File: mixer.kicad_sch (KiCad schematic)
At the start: 34 parts, among them T1 RF_BALUN, T2 RF_BALUN, U4 RFFC5072

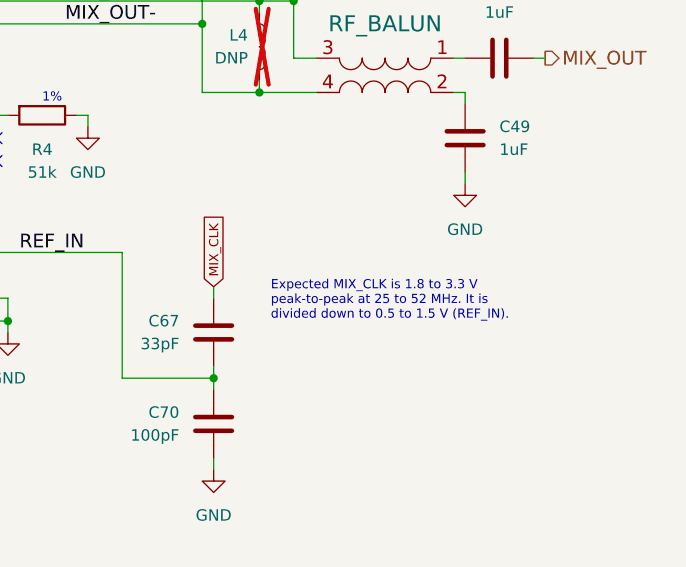
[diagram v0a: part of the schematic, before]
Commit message: Make clock source termination consistent
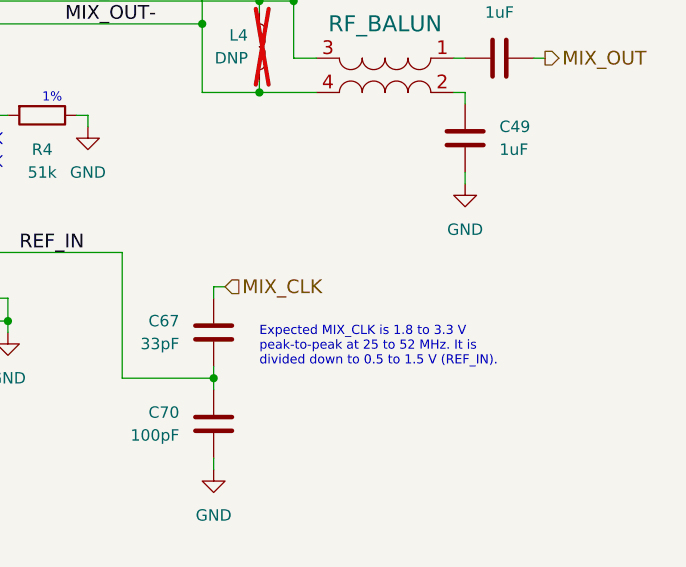
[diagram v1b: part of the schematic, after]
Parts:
- C67: footprint hackrf:GSG-0402 -> Capacitor_SMD:C_0201_0603Metric; Manufacturer Samsung -> Murata; Part Number CL05C330JB5NNNC -> GRM0335C1H330JA01D; Substitution Murata GRM1555C1H330JA01D -> GRM0335C1H330*, GRM0335C1E330*
- C70: footprint hackrf:GSG-0402 -> Capacitor_SMD:C_0201_0603Metric; Manufacturer Samsung -> Murata; Part Number CL05C101JB5NNNC -> GRM0335C1E101JA01D; Substitution Murata GRM1555C1H101JA01D -> GRM0335C1E101JA01*, GRM0335C1H101JA01*
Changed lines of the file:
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@@
 	(wire
 		(pts
+			(xy 151.13 118.11) (xy 152.4 118.11)
+		)
+		(stroke
+			(width 0)
+			(type default)
+		)
+	)
+	(wire
+		(pts
 			(xy 186.69 92.71) (xy 187.96 92.71)
 		)
@@
 	(text "Expected MIX_CLK is 1.8 to 3.3 V\npeak-to-peak at 25 to 52 MHz. It is\ndivided down to 0.5 to 1.5 V (REF_IN)."
 		(exclude_from_sim no)
-		(at 157.48 121.92 0)
+		(at 156.21 127 0)
 		(effects
 			(font
@@
 		)
 	)
-	(global_label "MIX_CLK"
+	(global_label "MIXER_RESETX"
 		(shape input)
-		(at 151.13 118.11 90)
+		(at 49.53 114.3 180)
 		(fields_autoplaced yes)
 		(effects
@@
 				(size 1.016 1.016)
 			)
-			(justify left)
+			(justify right)
 		)
 		(property "Intersheetrefs" "${INTERSHEET_REFS}"
-			(at 151.13 110.0042 90)
+			(at 36.7798 114.3 0)
 			(effects
 				(font
 					(size 1.27 1.27)
 				)
-				(justify left)
+				(justify right)
 				(hide yes)
 			)
 		)
 	)
-	(global_label "MIXER_RESETX"
+	(hierarchical_label "MIX_CLK"
 		(shape input)
-		(at 49.53 114.3 180)
+		(at 152.4 118.11 0)
 		(fields_autoplaced yes)
 		(effects
 			(font
-				(size 1.016 1.016)
-			)
-			(justify right)
-		)
-		(property "Intersheetrefs" "${INTERSHEET_REFS}"
-			(at 36.7798 114.3 0)
-			(effects
-				(font
-					(size 1.27 1.27)
-				)
-				(justify right)
-				(hide yes)
+				(size 1.524 1.524)
 			)
+			(justify left)
 		)
 	)
@@
 			)
 		)
-		(property "Footprint" "hackrf:GSG-0402"
+		(property "Footprint" "Capacitor_SMD:C_0201_0603Metric"
 			(at 151.13 123.19 0)
 			(effects
@@
 			)
 		)
-		(property "Description" "CAP CER 33PF 50V C0G/NP0 0402"
+		(property "Description" "CAP CER 33PF 50V C0G/NP0 0201"
 			(at -137.16 66.04 0)
 			(effects
@@
 			)
 		)
-		(property "Manufacturer" "Samsung"
+		(property "Manufacturer" "Murata"
 			(at -137.16 66.04 0)
 			(effects
@@
 			)
 		)
-		(property "Part Number" "CL05C330JB5NNNC"
+		(property "Part Number" "GRM0335C1H330JA01D"
 			(at -137.16 66.04 0)
 			(effects
@@
 			)
 		)
-		(property "Substitution" "Murata GRM1555C1H330JA01D"
+		(property "Substitution" "GRM0335C1H330*, GRM0335C1E330*"
 			(at 151.13 123.19 0)
 			(effects
@@
 			)
 		)
-		(property "Footprint" "hackrf:GSG-0402"
+		(property "Footprint" "Capacitor_SMD:C_0201_0603Metric"
 			(at 151.13 133.35 0)
 			(effects
@@
 			)
 		)
-		(property "Description" "CAP CER 100PF 50V 5% C0G/NP0 0402"
+		(property "Description" "CAP CER 100PF 25V C0G/NP0 0201"
 			(at 74.93 93.98 0)
 			(effects
@@
 			)
 		)
-		(property "Manufacturer" "Samsung"
+		(property "Manufacturer" "Murata"
 			(at 74.93 93.98 0)
 			(effects
@@
 			)
 		)
-		(property "Part Number" "CL05C101JB5NNNC"
+		(property "Part Number" "GRM0335C1E101JA01D"
 			(at 74.93 93.98 0)
 			(effects
@@
 			)
 		)
-		(property "Substitution" "Murata GRM1555C1H101JA01D"
+		(property "Substitution" "GRM0335C1E101JA01*, GRM0335C1H101JA01*"
 			(at 151.13 133.35 0)
 			(effects

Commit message: Change microcontroller U23 to LPC4330FET180
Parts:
- R5, R6: footprint hackrf:GSG-0402 -> Resistor_SMD:R_0402_1005Metric
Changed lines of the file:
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@@
 			)
 		)
-		(property "Footprint" "hackrf:GSG-0402"
+		(property "Footprint" "Resistor_SMD:R_0402_1005Metric"
 			(at 69.85 109.22 0)
 			(effects
@@
 			)
 		)
-		(property "Footprint" "hackrf:GSG-0402"
+		(property "Footprint" "Resistor_SMD:R_0402_1005Metric"
 			(at 78.74 109.22 0)
 			(effects

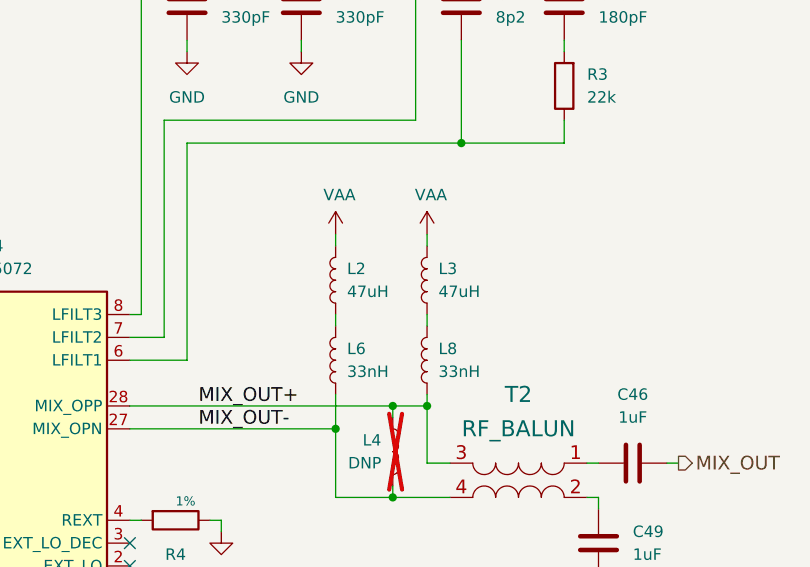
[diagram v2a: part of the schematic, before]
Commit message: Use single 15 uH inductor as RF choke
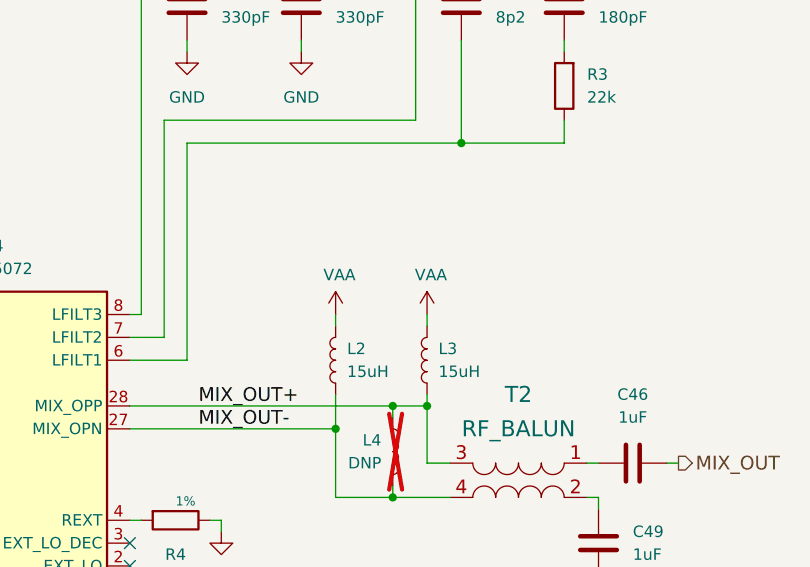
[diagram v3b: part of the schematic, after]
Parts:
- removed L6, L8: 33nH, Inductor_SMD:L_0201_0603Metric, symbol Device:L
- L2, L3: value 47uH -> 15uH; Part Number LSQNB160808T470M -> LSQPB160807T150M; Substitution LSQNB160808T470K -> BRL1608T150M, LLQPB160807T150M
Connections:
- net MIX_OUT+: now also L3.1
- net MIX_OUT-: now also L2.1
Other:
- moved on the sheet: L2, L3

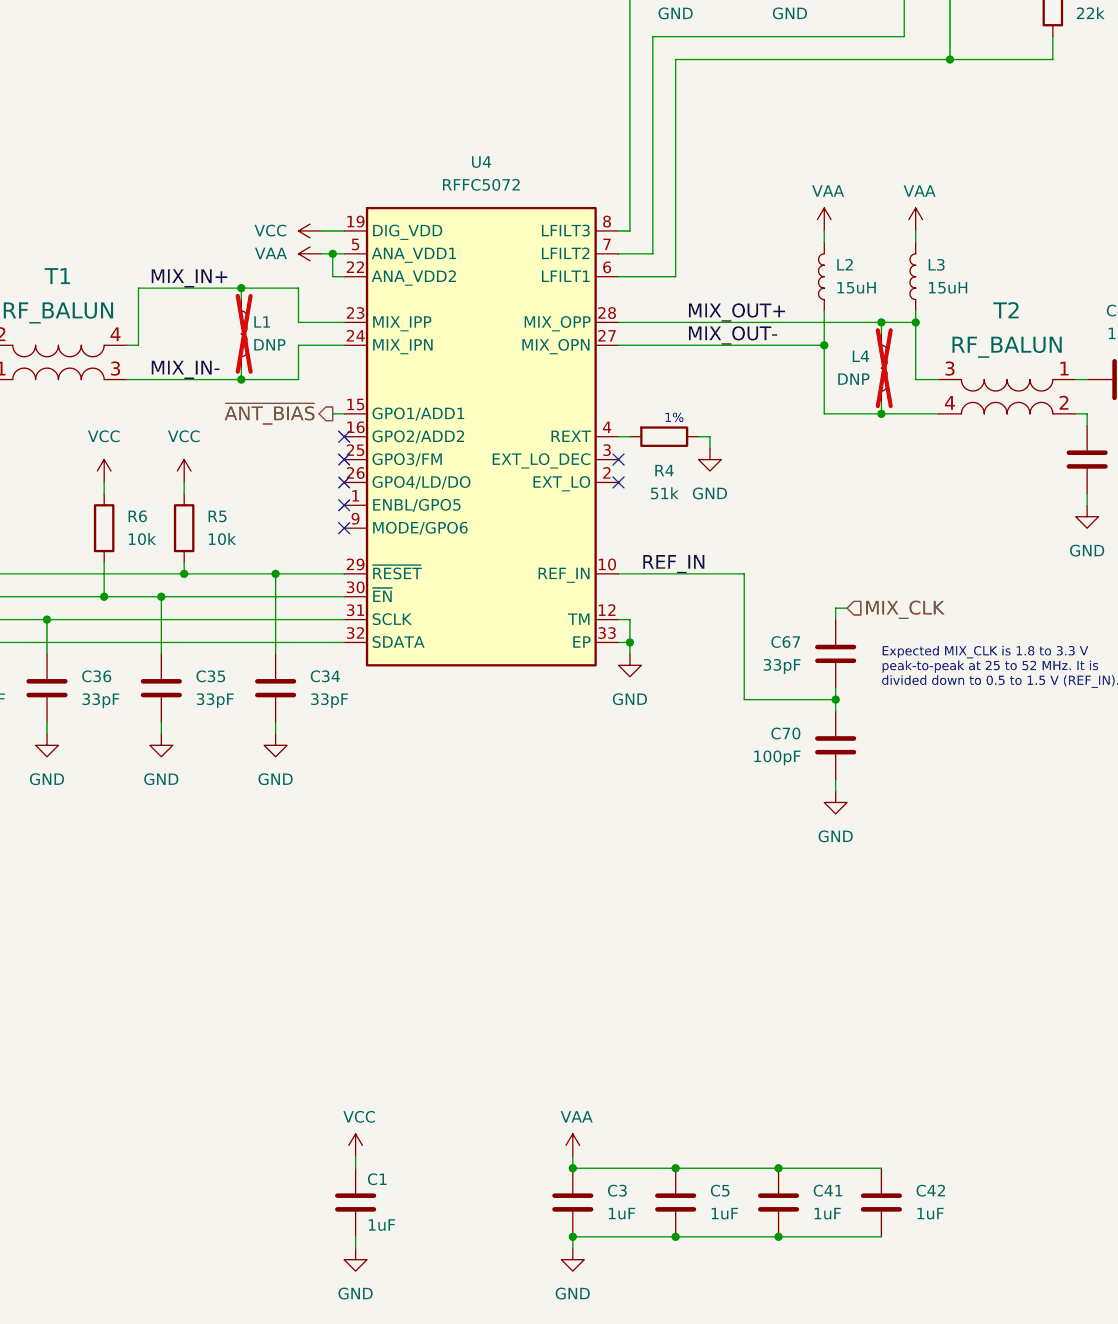
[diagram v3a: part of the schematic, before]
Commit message: Rearrange RF section
- Use DPDT RF switches to reduce long tracks
- Add limiter
- Add switch control logic
- Move ADC/DAC U18 to RF area
- Remove baseband header P9
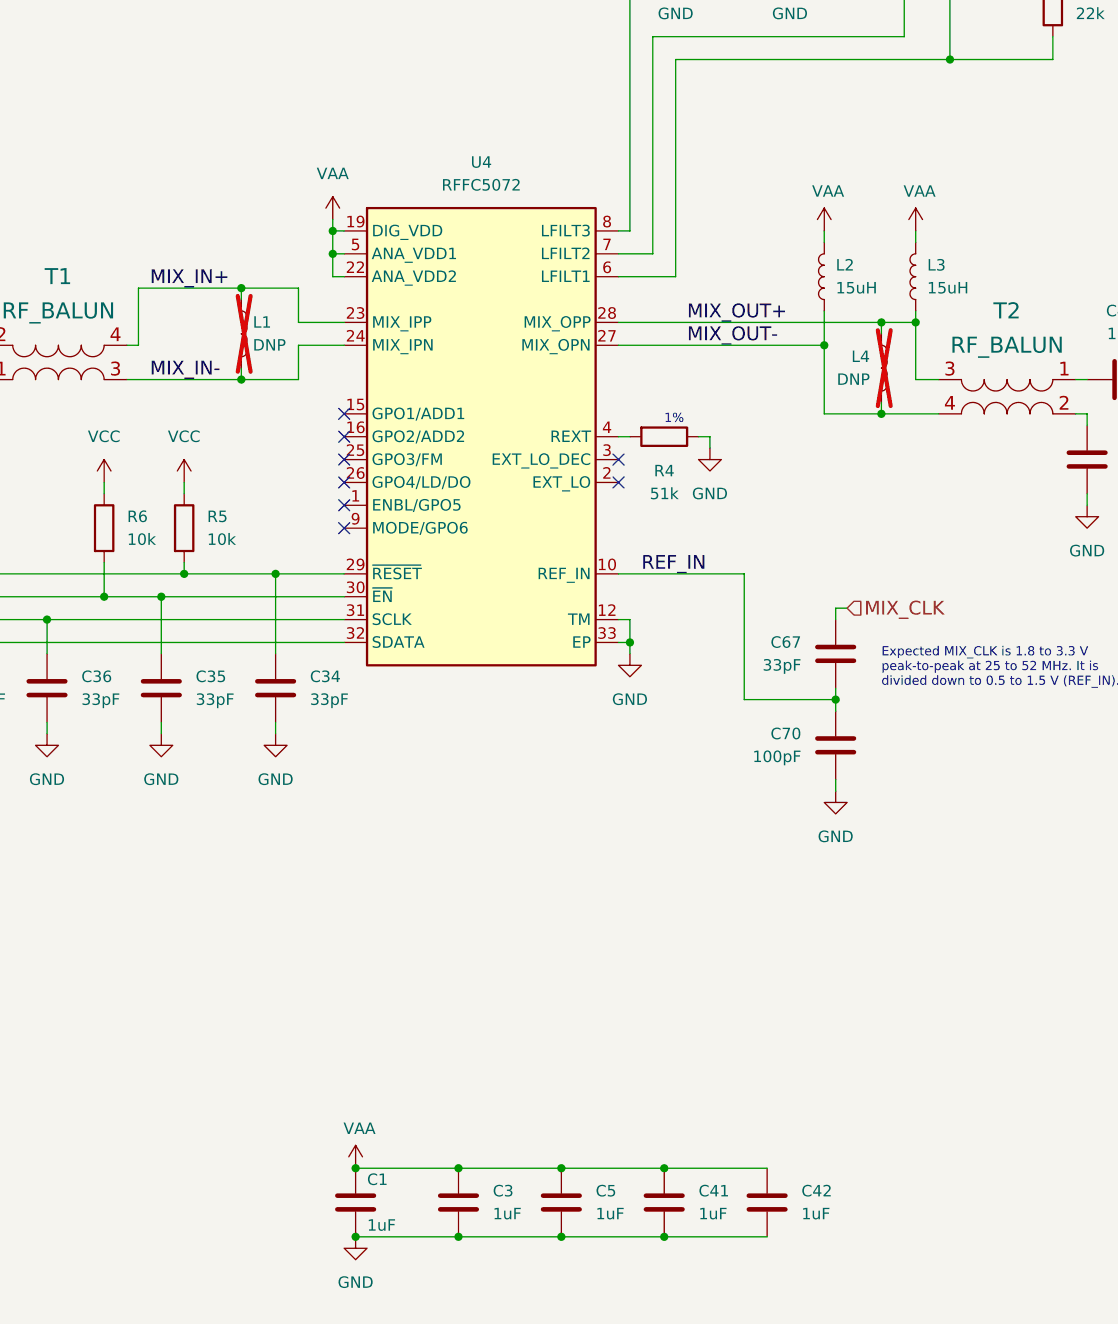
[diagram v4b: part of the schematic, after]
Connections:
- net VAA: now also C1.1, U4.19 (DIG_VDD)
- net VCC: no longer C1.1, U4.19 (DIG_VDD)
- net ~{ANT_BIAS}: no longer names the net of U4.15 (GPO1/ADD1)
- no-connect marks 7 -> 8
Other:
- moved on the sheet: C3, C41, C42, C5

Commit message: Change Type-C controller U29 to HUSB328
- Update USB TVS
- Improve USB differential impedance
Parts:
- R3: Part Number RC0201JR-0722KL -> RC0201FR-0722K6L
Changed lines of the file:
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@@
 			)
 		)
-		(property "Description" "RES 22K OHM 5% 1/20W 0201"
+		(property "Description" "RES 22.6K OHM 1% 1/20W 0201"
 			(at 175.26 50.8 0)
 			(effects
@@
 			)
 		)
-		(property "Part Number" "RC0201JR-0722KL"
+		(property "Part Number" "RC0201FR-0722K6L"
 			(at 175.26 50.8 0)
 			(effects

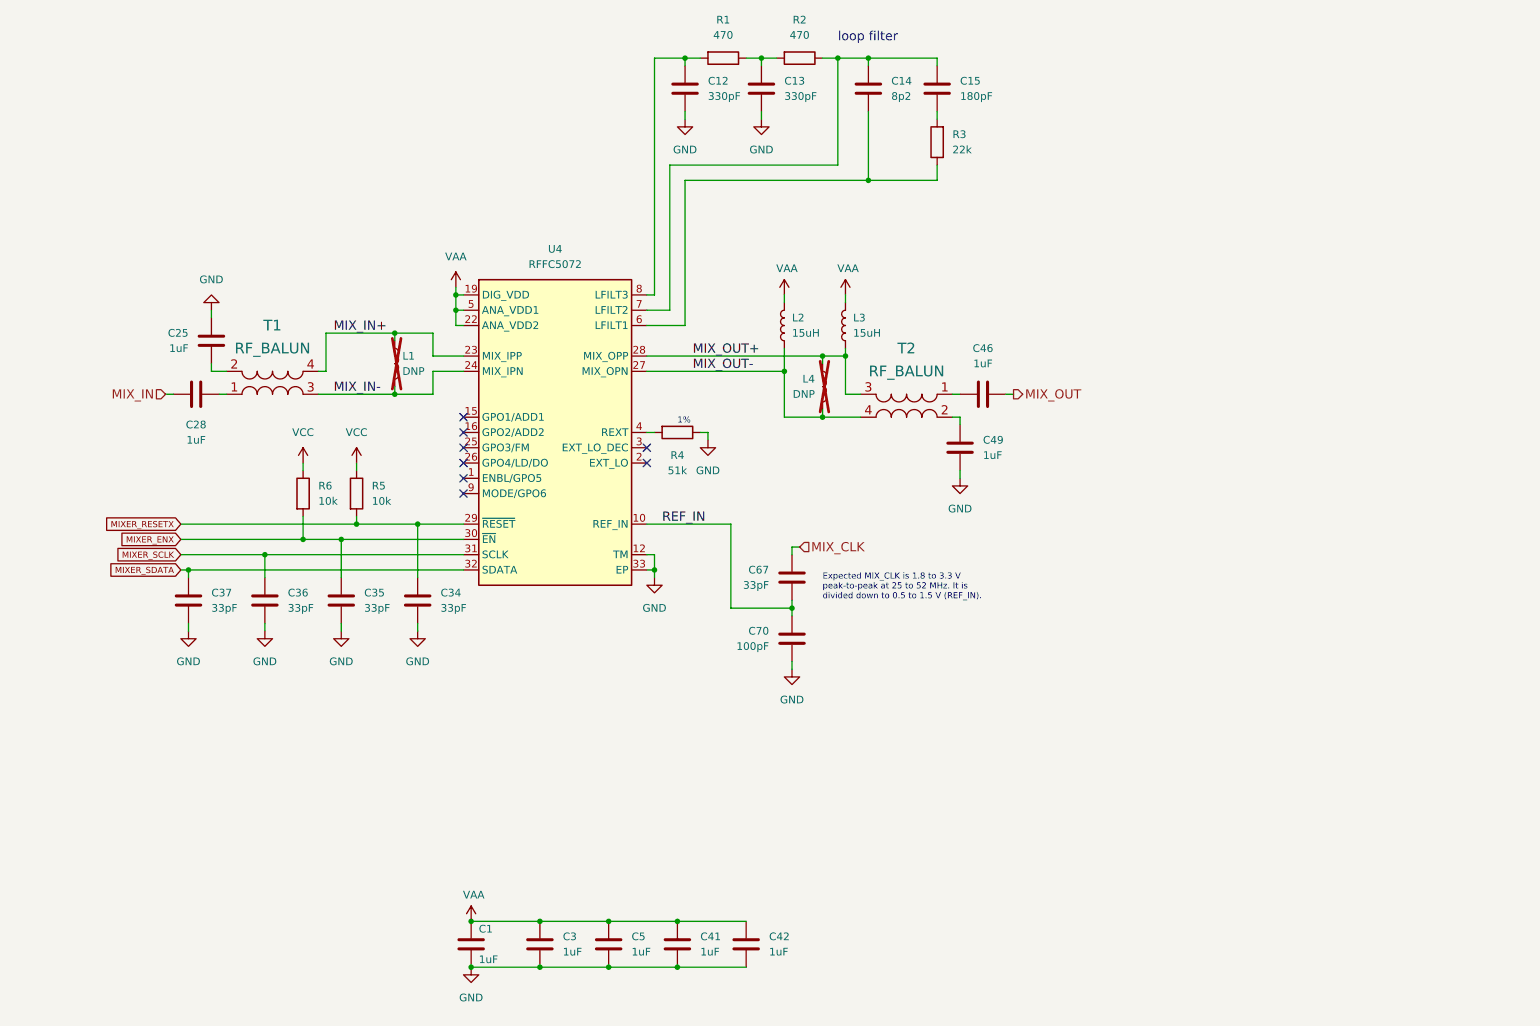
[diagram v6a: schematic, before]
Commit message: Connect mixer U4 LD and ENBL pins to MCU
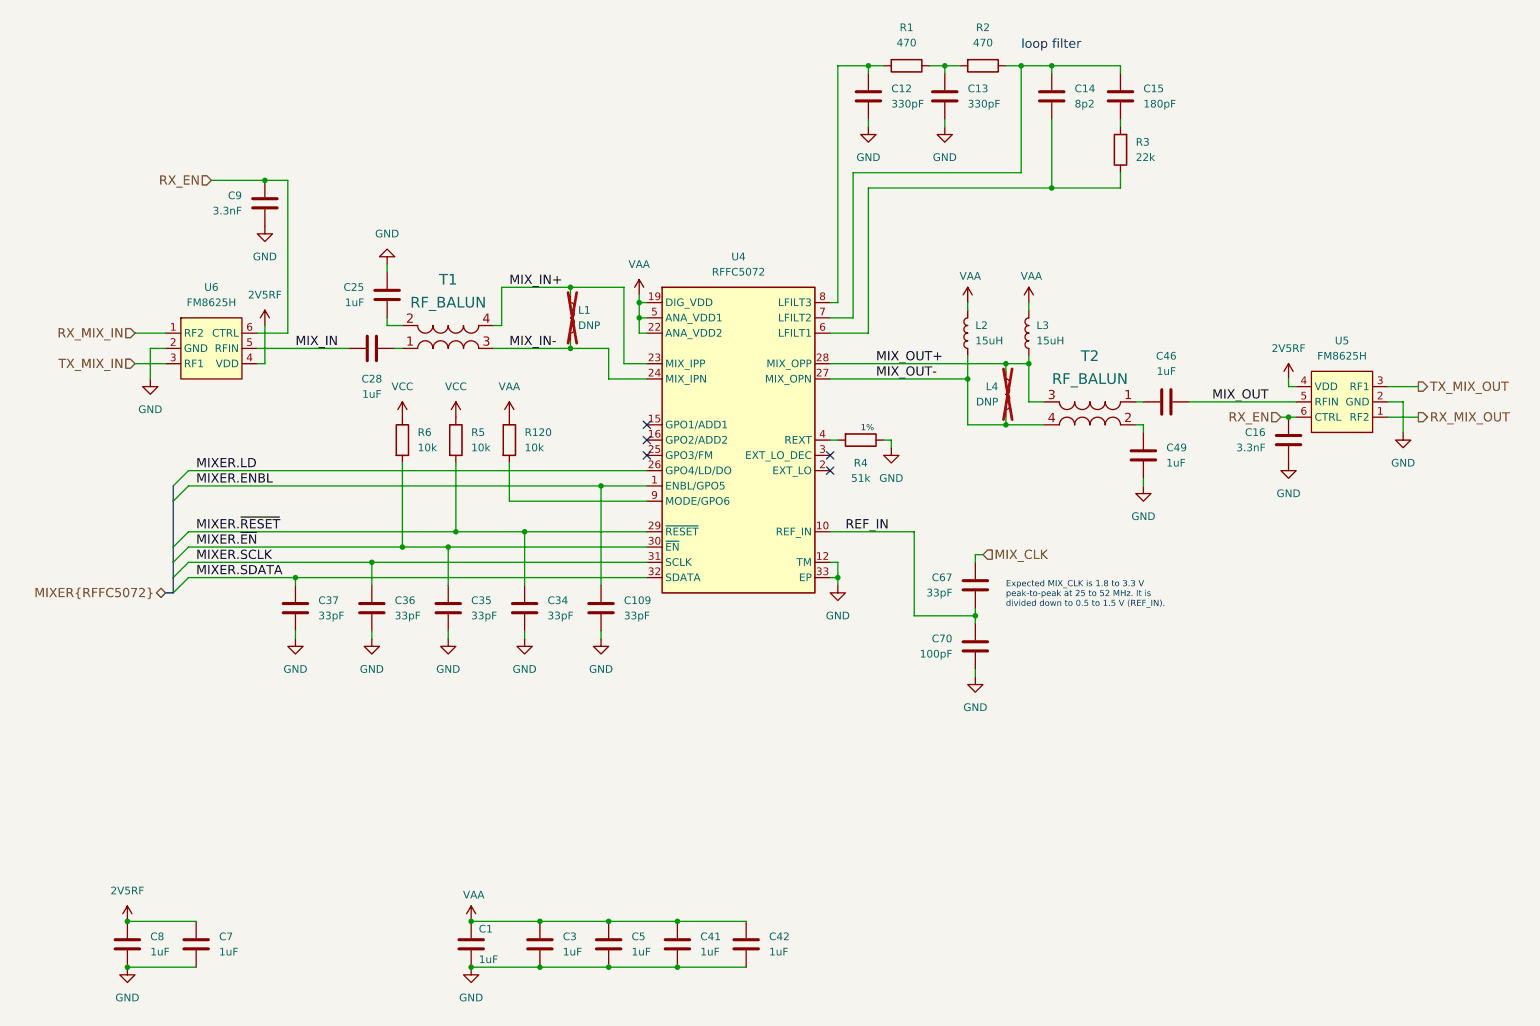
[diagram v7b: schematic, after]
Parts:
- added C109: 33pF, Capacitor_SMD:C_0201_0603Metric, symbol Device:C
- added C16, C9: 3.3nF, Capacitor_SMD:C_0201_0603Metric, symbol Device:C
- added C7, C8: 1uF, Capacitor_SMD:C_0201_0603Metric, symbol Device:C
- added R120: 10k, Resistor_SMD:R_0402_1005Metric, symbol Device:R
- added U5, U6: FM8625H, praline:TSLP-6-4_1.1x0.7mm_P0.4mm, symbol praline:BGS12P2L6
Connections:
- net GND: now also C109.2, C16.1, C7.2, C8.2, C9.1, U5.2 (GND), U6.2 (GND)
- net MIX_IN: now also U6.5 (RFIN)
- net MIX_OUT: now also U5.5 (RFIN)
- net VAA: now also R120.1
- net MIXER.ENBL: now reaches U4.1 (ENBL/GPO5)
- net MIXER.ENBL: now also C109.1
- net MIXER.LD: now reaches U4.26 (GPO4/LD/DO)
- net at U4.9 (MODE/GPO6): now also R120.2
- net MIXER_ENX renamed MIXER.~{EN}
- net MIXER_RESETX renamed MIXER.~{RESET}
- net MIXER_SCLK renamed MIXER.SCLK
- net MIXER_SDATA renamed MIXER.SDATA
- new net 2V5RF: C7.1, C8.1, U5.4 (VDD), U6.4 (VDD)
- new net RX_EN: C16.2, C9.2, U5.6 (CTRL), U6.6 (CTRL)
- new net RX_MIX_IN: U6.1 (RF2)
- new net RX_MIX_OUT: U5.1 (RF2)
- new net TX_MIX_IN: U6.3 (RF1)
- new net TX_MIX_OUT: U5.3 (RF1)
- no-connect marks 8 -> 5
